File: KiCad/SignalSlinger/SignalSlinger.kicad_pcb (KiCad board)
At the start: 2 copper layers, 94.1 x 59.1 mm, 121 parts, among them J101 Conn_01x02, J102 Conn_01x03, J103 Conn_01x02, J104 Conn_01x02, J105 Conn_01x04, J106 Conn_01x02, J107 DB9 Female, J109 SolderJumper_2_Bridged, J201 Barrel_Jack_Switch, J203 External Fan Power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

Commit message: Ver 2.4
Minor schematic update.
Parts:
- C217: value 330nF -> 470nF
- C302, C305: value C_0805_2012Metric -> 1100pF
- C303: value C_0805_2012Metric -> 1800pF
- C304: value C_0805_2012Metric -> 91pF
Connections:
- C111 pad 1: Net-(C111-Pad1) -> Net-(C112-Pad2)
- C112 pad 2: Net-(C111-Pad1) -> Net-(C112-Pad2)
- D113 pad 2: Net-(C111-Pad1) -> Net-(C112-Pad2)
- D114 pad 1: Net-(C111-Pad1) -> Net-(C112-Pad2)
- D115 pad 2: V_ext -> Net-(C112-Pad2)
- J109 pad 2: Net-(C111-Pad1) -> Net-(C112-Pad2)
- L101 pad 1: Net-(C111-Pad1) -> Net-(C112-Pad2)
- R2 pad 2: Net-(C111-Pad1) -> Net-(C112-Pad2)
- U105 pad 2: Net-(C111-Pad1) -> Net-(C112-Pad2)
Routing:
- net Net-(C112-Pad2): track 0.00 -> 76.8 mm
- net Net-(C111-Pad1): track 59.9 -> 0.00 mm
- net V_ext: track 164.0 -> 160.3 mm, vias 9 -> 7
- added copper zone on F.Cu, net Net-(C112-Pad2)
- removed copper zone on F.Cu, net Net-(C111-Pad1)

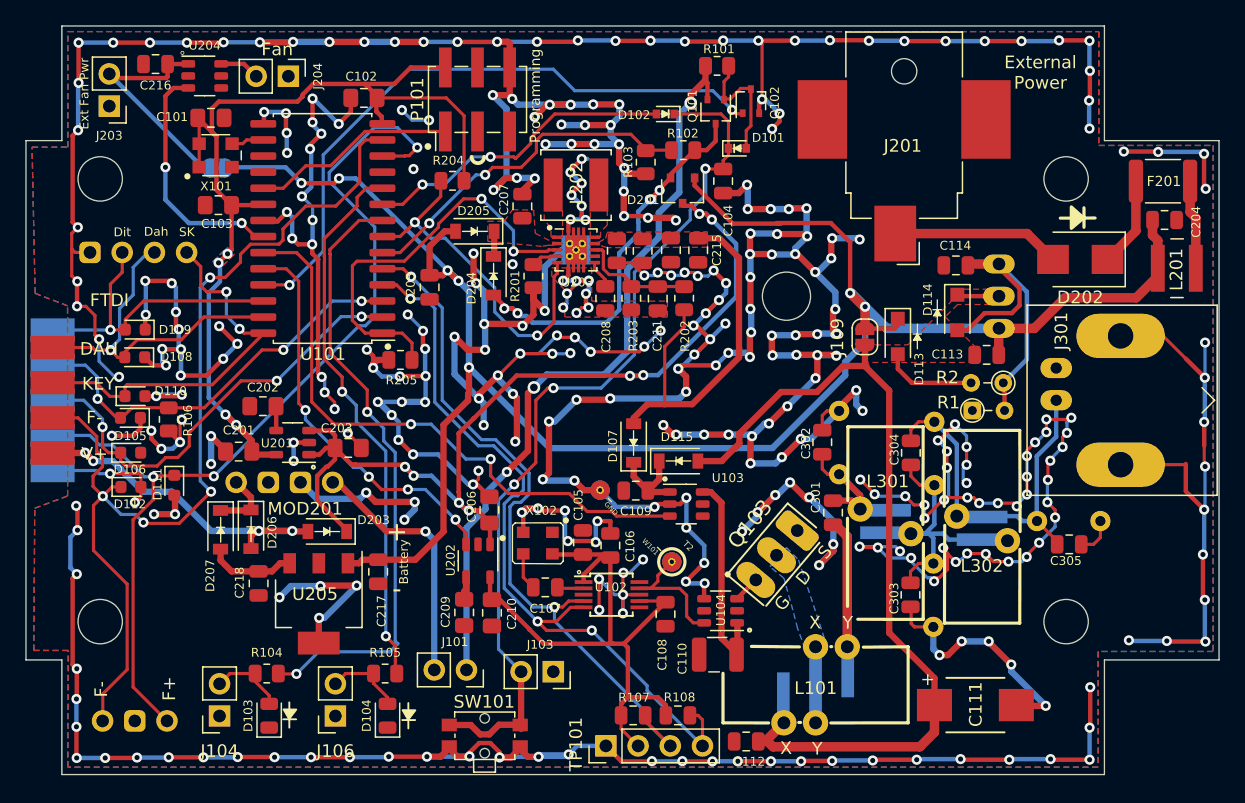
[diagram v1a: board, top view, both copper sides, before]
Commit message: Added voltage divider
Now supports monitoring external battery voltage.
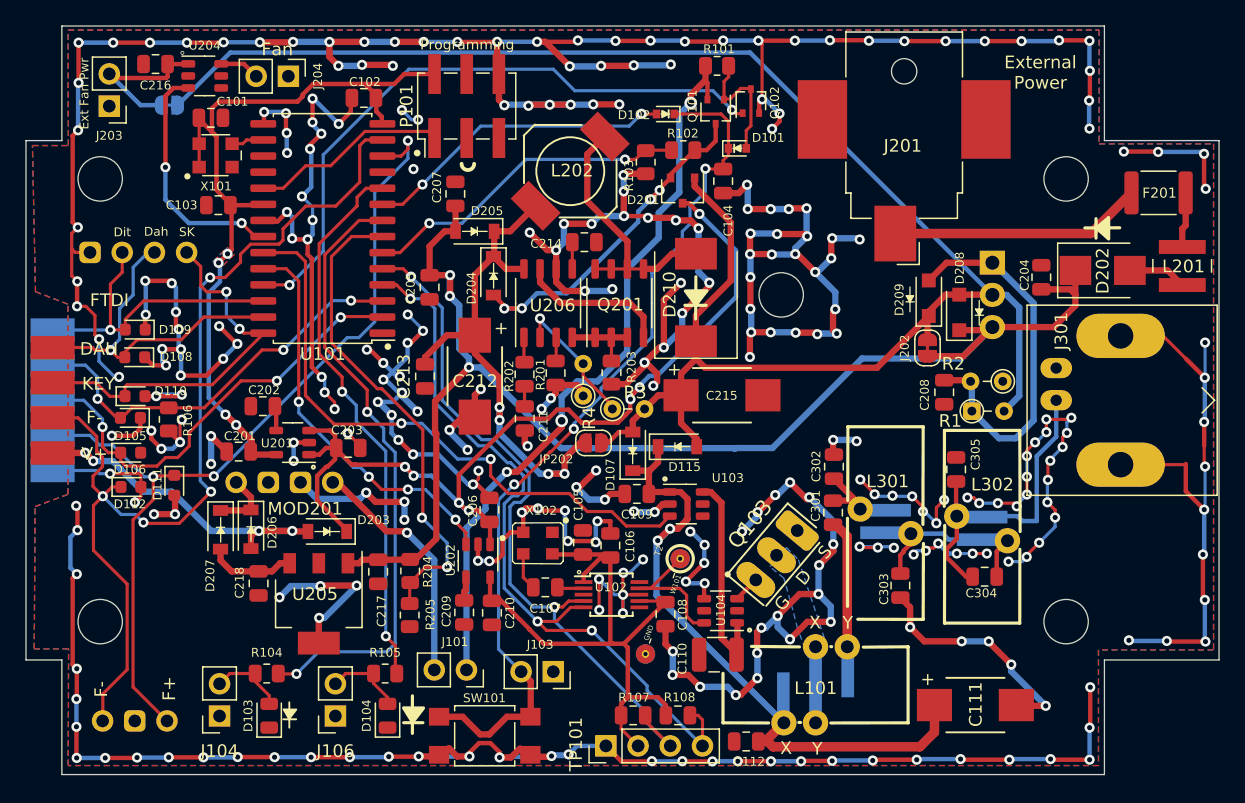
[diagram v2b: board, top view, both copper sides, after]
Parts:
- removed C113, C114: 10uF, Capacitor_SMD:C_0805_2012Metric
- removed C302x, C305x: 1100pF, Capacitor_THT:C_Rect_L7.0mm_W2.5mm_P5.00mm
- removed C303x: 1800pF, Capacitor_THT:C_Rect_L7.0mm_W2.5mm_P5.00mm
- removed C304x: 91pF, Capacitor_THT:C_Rect_L7.0mm_W2.5mm_P5.00mm
- removed D113, D114: 1N4001, Diode_SMD:D_SOD-123F
- removed J109: SolderJumper_2_Bridged, Jumper:SolderJumper-2_P1.3mm_Bridged_RoundedPad1.0x1.5mm
- removed the U203 at (89.4, 77.5)
- added D208: 1N4001, Diode_SMD:D_SOD-123F, F.Cu at (119.6, 82.5)
- added D209: 1N4001, Diode_SMD:D_SOD-123F, F.Cu at (117.2, 81.4)
- added D210: B530, Diode_SMD:D_SMC, F.Cu at (98.8, 81.3)
- added J202: SolderJumper_2_Bridged, Jumper:SolderJumper-2_P1.3mm_Bridged_RoundedPad1.0x1.5mm, F.Cu at (117.1, 85.3)
- added JP202: Boost Bypass, Jumper:SolderJumper-2_P1.3mm_Open_RoundedPad1.0x1.5mm, F.Cu at (90.8, 92.8)
- added Q201: RJK0354DSP, Package_SO:SOIC-8_3.9x4.9mm_P1.27mm, F.Cu at (92.8, 81.8)
- added R3: TBD, Resistor_THT:R_Axial_DIN0204_L3.6mm_D1.6mm_P2.54mm_Vertical, F.Cu at (92.3, 90.1)
- added R4: TBD, Resistor_THT:R_Axial_DIN0204_L3.6mm_D1.6mm_P2.54mm_Vertical, F.Cu at (90.0, 89.1)
- added U206: MIC2196, Package_SO:SOIC-8_3.9x4.9mm_P1.27mm, F.Cu at (87.2, 81.8)
- C101, C102, C103, C201, C202, C203, C206, C209, C210: footprint Capacitor_SMD:C_0805_2012Metric_Pad1.18x1.45mm_HandSolder -> Capacitor_SMD:C_0805_2012Metric
- C208: value 100nF -> 10uF
- C211: value 10pF -> 10nF
- C212: value 1uF -> 47uF low ESR; footprint Capacitor_SMD:C_0805_2012Metric -> Capacitors:C_2917
- C213: value 22uF -> 10uF
- C214: value 22uF -> 1uF
- C215: value 22uF -> 47uF low ESR; footprint Capacitor_SMD:C_0805_2012Metric -> Capacitors:C_2917
- L202: value 1uH -> 6.8uH; footprint Inductor_SMD:L_Bourns_SRN5040TA -> Inductors:CDR7D28MN
- R201: value 105k -> 10k; footprint Resistor_SMD:R_0805_2012Metric -> Capacitor_SMD:C_0805_2012Metric
- R202: value 1M -> 10k; footprint Resistor_SMD:R_0805_2012Metric -> Capacitor_SMD:C_0805_2012Metric
- R203: value 80.6k -> 0.01 0.5W
- R204: value 1M -> 162k
- R205: value 105k -> 12.4k
- SW101: footprint Button_Switch_SMD:SW_SPST_TL1014BF160QG -> Button_Switch_SMD:SW_SPST_TL3305A
- U203: renamed from U105; footprint TO_SOT_Packages:TO-220_Neutral123_Horizontal -> Package_TO_SOT_THT:TO-220-3_Horizontal_TabDown
- moved R204 31.0 mm to (76.3, 102.9), turned to 90 degrees
- moved C208 27.7 mm to (118.4, 88.8)
- moved R205 20.1 mm to (76.3, 106.4), turned to 90 degrees
- moved C213 19.8 mm to (77.5, 87.5), turned to -90 degrees
- moved C212 14.9 mm to (81.4, 87.5)
- moved C211 14.1 mm to (85.3, 90.8)
- moved R202 13.9 mm to (85.3, 87.4)
- moved C215 11.6 mm to (100.9, 89.0), turned to 0 degrees
- moved C304 11.4 mm to (121.6, 103.3), turned to 0 degrees
- moved C204 10.7 mm to (126.1, 79.7), turned to -90 degrees
- moved C305 10.7 mm to (119.4, 94.9), turned to 90 degrees
- moved R201 7.84 mm to (87.8, 87.3), turned to 90 degrees
- moved C214 6.86 mm to (90.0, 76.9), turned to 0 degrees
- moved JP201 6.24 mm to (57.3, 66.1)
- moved R203 6.07 mm to (92.2, 87.2), turned to 90 degrees
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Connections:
- C111 pad 1: Net-(C112-Pad2) -> Net-(C109-Pad2)
- C112 pad 2: Net-(C112-Pad2) -> Net-(C109-Pad2)
- C207 pad 2: Net-(C207-Pad2) -> V_ext
- C212 pad 1: +7V -> Net-(C212-Pad1)
- C213 pad 1: GND -> Net-(C212-Pad1)
- C213 pad 2: +7V -> GND
- C214 pad 1: GND -> Net-(C214-Pad1)
- C214 pad 2: +7V -> GND
- C215 pad 1: GND -> Vdrive
- C215 pad 2: +7V -> GND
- D107 pad 2: +7V -> Vdrive
- D115 pad 2: Net-(C112-Pad2) -> Vdrive
- D201 pad 1: V_ext -> Vdrive
- D202 pad 1: Net-(D202-Pad1) -> V_ext
- D204 pad 1: Net-(C207-Pad2) -> Net-(C212-Pad1)
- D205 pad 1: Net-(C207-Pad2) -> Net-(C212-Pad1)
- F201 pad 2: Net-(D202-Pad1) -> Net-(F201-Pad2)
- J201 pad 1: Net-(D202-Pad2) -> Net-(F201-Pad2)
- JP201 pad 1: V_ext -> Vdrive
- L101 pad 1: Net-(C112-Pad2) -> Net-(C109-Pad2)
- L201 pad 2: V_ext -> Net-(D202-Pad2)
- L202 pad 2: Net-(L202-Pad2) -> Net-(C212-Pad1)
- R1 pad 1: GND -> Net-(C208-Pad1)
- R1 pad 2: Net-(C114-Pad1) -> Vdrive
- R2 pad 1: Net-(C114-Pad1) -> GND
- R2 pad 2: Net-(C112-Pad2) -> Net-(C208-Pad1)
- R201 pad 1: Net-(R201-Pad1) -> GND
- R201 pad 2: GND -> BOOST_PWR_ENABLE
- R202 pad 1: +7V -> Net-(C211-Pad1)
- R202 pad 2: Net-(C211-Pad1) -> Net-(R202-Pad2)
- R203 pad 1: Net-(C211-Pad1) -> GND
- R203 pad 2: GND -> Net-(Q201-Pad1)
- R204 pad 1: +3V3 -> Vext
- R204 pad 2: Power_Good -> V_ext
- R205 pad 2: B/B_PS_Enable -> Vext
- U101 pad 7: Power_Good -> Vext
- U203 pad 1: Net-(C114-Pad1) -> Net-(C208-Pad1)
- U203 pad 2: Net-(C112-Pad2) -> Vdrive
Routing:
- net Vdrive: track 0.00 -> 147.5 mm
- net GND: track 901.4 -> 787.1 mm, vias 355 -> 308
- net Net-(C112-Pad2): track 76.8 -> 0.00 mm
- net V_ext: track 160.3 -> 109.6 mm, vias 7 -> 3
- net Net-(C109-Pad2): track 7.18 -> 52.0 mm, vias 0 -> 2
- net Net-(C212-Pad1): track 0.00 -> 41.4 mm, vias 0 -> 4
- net Vext: track 0.00 -> 38.3 mm, vias 0 -> 2
- net B/B_PS_Enable: track 32.1 -> 0.00 mm, vias 2 -> 0
- net +7V: track 30.6 -> 0.00 mm
- net Power_Good: track 28.4 -> 0.00 mm, vias 2 -> 0
- net Net-(C208-Pad1): track 2.23 -> 29.9 mm
- net Net-(C114-Pad1): track 24.8 -> 0.00 mm
- net Net-(D210-Pad2): track 0.00 -> 20.8 mm
- net Net-(F201-Pad2): track 0.00 -> 20.0 mm
- net +3V3: track 77.1 -> 63.4 mm
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- removed copper zone on F.Cu, net +7V
- removed copper zone on F.Cu, net Net-(C112-Pad2)
- removed copper zone on F.Cu, net Net-(C207-Pad2)
- removed copper zone on F.Cu, net Net-(D210-Pad2)
- removed copper zone on F.Cu, net Net-(L202-Pad2)
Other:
- board text removed: "+"
- board text removed: "-"
- board text removed: "Battery"
- board text removed: "PS Heat Sink"

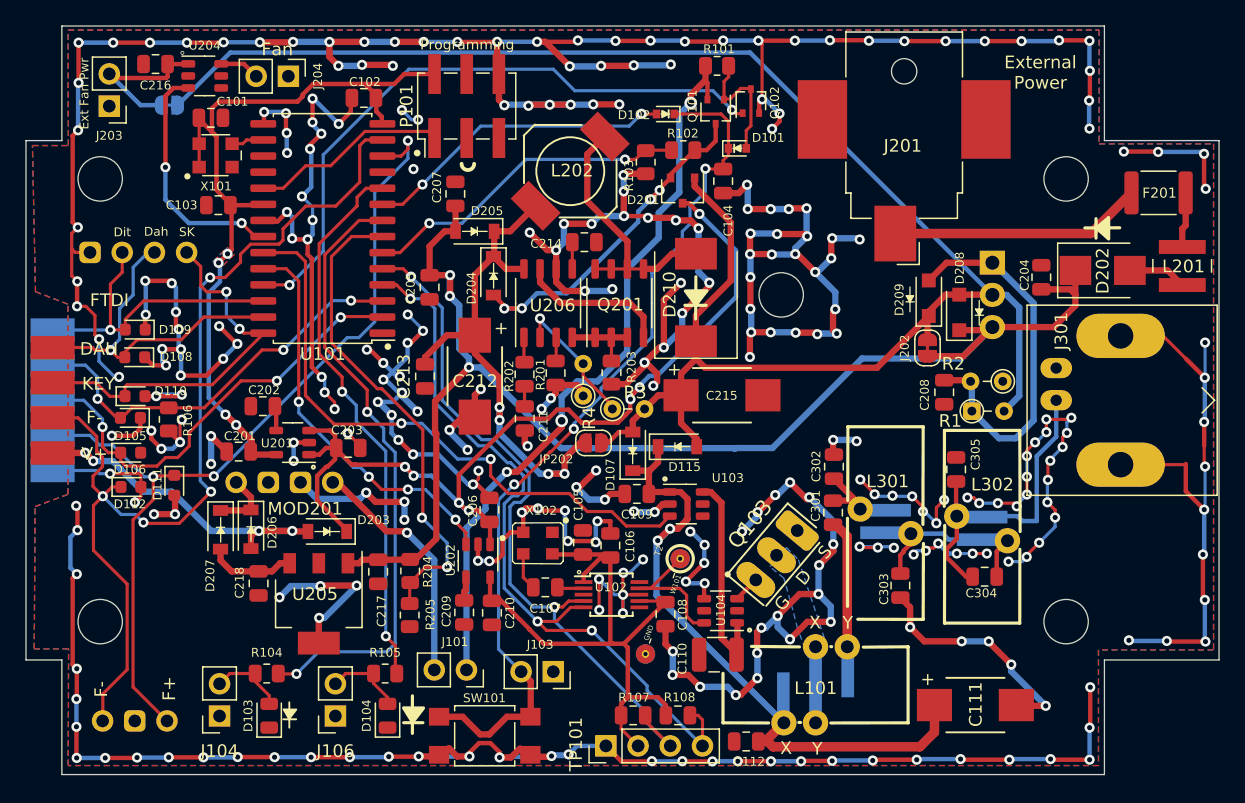
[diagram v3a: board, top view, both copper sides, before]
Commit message: Extensive Cleanup
BOM scrub
Added jumpers for foxoring power level
PCB ground plane improvements
Updated Gerbers
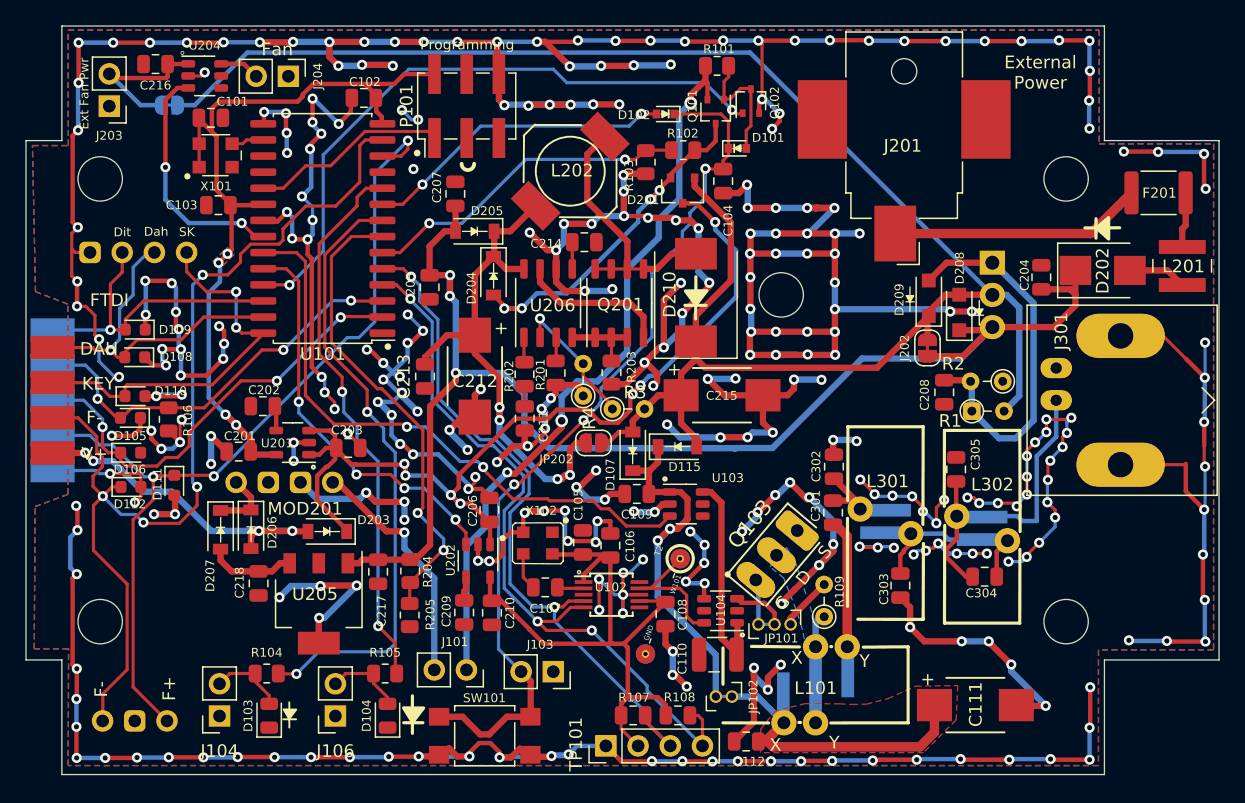
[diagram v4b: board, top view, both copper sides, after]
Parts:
- added JP101: NetTie_Jumper_3_Bridged12, Jumper:Jumper_THT_1x03_Bridged12_P1.27mm_Vertical, F.Cu at (105.1, 107.1)
- added JP102: NetTie_Jumper_2_Bridged, Jumper:Jumper_THT_1x02_P1.27mm_Vertical, F.Cu at (101.7, 112.8)
- added R109: 47 0.5W, Resistor_THT:R_Axial_DIN0204_L3.6mm_D1.6mm_P2.54mm_Vertical, F.Cu at (109.0, 106.5)
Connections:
- C111 pad 1: Net-(C109-Pad2) -> Net-(C111-Pad1)
- C112 pad 2: Net-(C109-Pad2) -> Net-(C111-Pad1)
- L101 pad 1: Net-(C109-Pad2) -> Net-(C111-Pad1)
- U104 pad 3: Net-(Q103-Pad1) -> Net-(U104-Pad3)
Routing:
- net GND: track 787.1 -> 831.0 mm, vias 308 -> 319
- net Net-(C111-Pad1): track 0.00 -> 23.6 mm
- net Net-(C109-Pad2): track 52.0 -> 29.0 mm
- net Net-(R109-Pad2): track 0.00 -> 4.24 mm
- net Net-(U104-Pad3): track 0.00 -> 4.03 mm
- net Net-(L101-Pad2): track 0.00 -> 2.54 mm
- net V_ext: track 109.6 -> 110.8 mm
- net Net-(Q103-Pad1): track 2.09 -> 3.30 mm
- net Vext: track 38.3 -> 37.4 mm
- net Net-(R108-Pad1): track 59.8 -> 58.9 mm
- net FET_DRIVER_ENABLE: track 48.3 -> 47.6 mm
- net Net-(C212-Pad1): track 41.4 -> 42.1 mm
- net Straightkey: track 30.0 -> 30.5 mm
- added copper zone on F.Cu, net Net-(C111-Pad1)

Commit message: Four Layers
Changed to a four-layer board, mostly for thermal flow reasons, but it also significantly improves ground plane coverage and voltage routing.
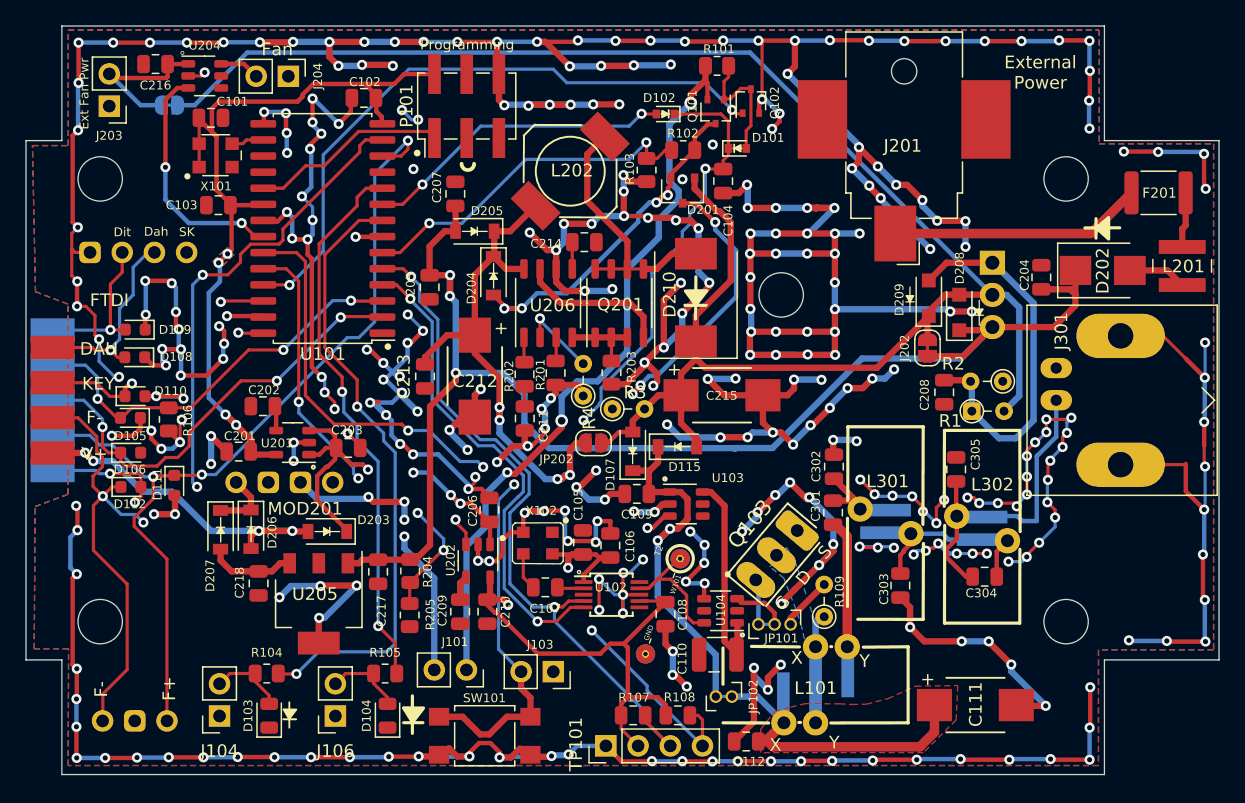
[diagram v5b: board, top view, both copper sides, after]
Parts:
- moved R103 0.62 mm to (95.0, 71.2)
- moved C210 0.37 mm to (82.4, 106.1)
- moved C209 0.33 mm to (80.2, 106.1)
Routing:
- net GND: track 831.0 -> 889.0 mm, vias 319 -> 339
- net VDD: track 47.6 -> 58.0 mm, vias 0 -> 2
- net Net-(C203-Pad2): track 74.4 -> 77.3 mm
- net Vbat: track 26.2 -> 28.0 mm
- net Frequency Down: track 80.0 -> 78.7 mm
- net Straightkey: track 30.5 -> 29.3 mm
- net Paddle_Dit: track 24.3 -> 25.0 mm, vias 1 -> 2
- net Net-(J101-Pad1): track 58.4 -> 59.1 mm
- net Paddle Dah: track 27.3 -> 27.8 mm, vias 1 -> 2
- net Vext: track 37.4 -> 37.1 mm, vias 2 -> 3
- net V3V3_PWR_ENABLE: track 31.9 -> 32.0 mm, vias 4 -> 3
- net FET_DRIVER_ENABLE: vias 2 -> 3
- added copper zone on In1.Cu, net GND
- added copper zone on In2.Cu, net GND
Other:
- copper layers 2 -> 4

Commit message: Schematic and PCB Update
Added jumpers for Foxoring operation
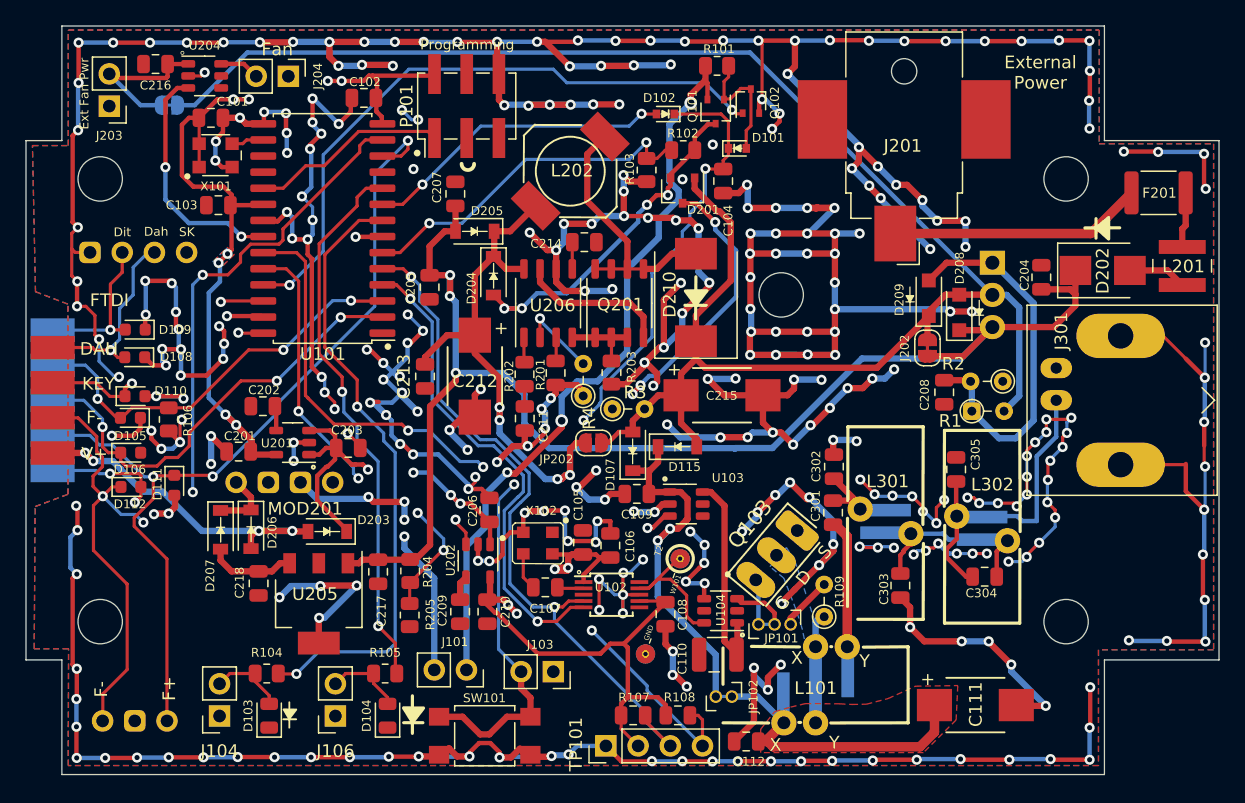
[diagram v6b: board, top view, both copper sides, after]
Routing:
- net +3V3: track 63.4 -> 76.1 mm, vias 4 -> 8
- net GND: track 889.0 -> 897.2 mm, vias 339 -> 342
- net VDD: track 58.0 -> 59.7 mm, vias 2 -> 4
- net +VSW: track 28.2 -> 29.0 mm
